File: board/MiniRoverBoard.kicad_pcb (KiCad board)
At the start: 2 copper layers, 103.4 x 63.8 mm, 49 parts, among them J1 DEBUG, Q1 NMOS, Q2 BSS138, U2 OKI, U3 Opamp_Dual, U4 LT1910, U7 ESP32-S2-DEVKITM-1U, U8 Opamp_Dual

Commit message: Corrected 5 volt power grid
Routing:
- net GND: vias 9 -> 17
- added copper zone on F.Cu, net GND
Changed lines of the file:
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@@
+	)
+	(via
+		(at 117.602 70.104)
+		(size 0.6)
+		(drill 0.3)
+		(layers "F.Cu" "B.Cu")
+		(free yes)
+		(net 1)
+	)
+	(via
+		(at 128.27 62.484)
+		(size 0.6)
+		(drill 0.3)
+		(layers "F.Cu" "B.Cu")
+		(free yes)
+		(net 1)
 	)
 	(via
@@
 	)
 	(via
+		(at 122.682 74.422)
+		(size 0.6)
+		(drill 0.3)
+		(layers "F.Cu" "B.Cu")
+		(free yes)
+		(net 1)
+	)
+	(via
+		(at 128.016 55.88)
+		(size 0.6)
+		(drill 0.3)
+		(layers "F.Cu" "B.Cu")
+		(free yes)
+		(net 1)
+	)
+	(via
 		(at 100.838 52.07)
+		(size 0.6)
+		(drill 0.3)
+		(layers "F.Cu" "B.Cu")
+		(free yes)
+		(net 1)
+	)
+	(via
+		(at 146.05 78.74)
 		(size 0.6)
 		(drill 0.3)
@@
 	)
 	(via
+		(at 127 75.184)
+		(size 0.6)
+		(drill 0.3)
+		(layers "F.Cu" "B.Cu")
+		(free yes)
+		(net 1)
+	)
+	(via
 		(at 107.442 52.07)
 		(size 0.6)
@@
 	)
 	(via
+		(at 132.334 66.04)
+		(size 0.6)
+		(drill 0.3)
+		(layers "F.Cu" "B.Cu")
+		(free yes)
+		(net 1)
+	)
+	(via
+		(at 137.16 83.058)
+		(size 0.6)
+		(drill 0.3)
+		(layers "F.Cu" "B.Cu")
+		(free yes)
+		(net 1)
+	)
+	(via
 		(at 58.928 55.626)
 		(size 0.6)
@@
 		(net 3)
 		(net_name "+5V")
+		(layer "F.Cu")
+		(hatch edge 0.5)
+		(priority 3)
+		(connect_pads yes
+			(clearance 0.254)
+		)
+		(min_thickness 0.254)
+		(filled_areas_thickness no)
+		(fill yes
+			(thermal_gap 0.5)
+			(thermal_bridge_width 0.5)
+		)
+		(polygon
+			(pts
+				(xy 117.856 72.136) (xy 117.7055 76.2) (xy 121.158 76.2) (xy 121.666 72.136)
+			)
+		)
+	)
+	(zone
+		(net 1)
+		(net_name "GND")
 		(layer "F.Cu")
 		(hatch edge 0.5)
@@
 		(polygon
 			(pts
-				(xy 117.602 72.282267) (xy 121.412 72.368724) (xy 121.412 76.2) (xy 117.602 76.2)
+				(xy 170.18 72.282267) (xy 173.99 72.368724) (xy 173.99 76.2) (xy 170.18 76.2)
 			)
 		)

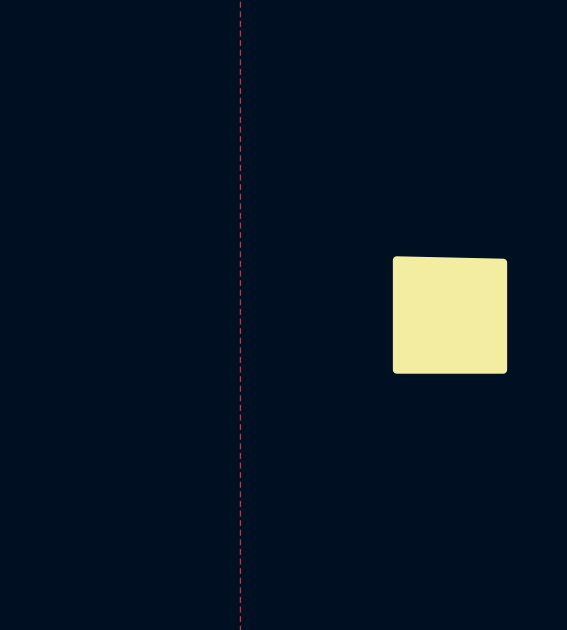
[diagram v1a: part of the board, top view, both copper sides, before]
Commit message: Removed extra 5 volt power grid
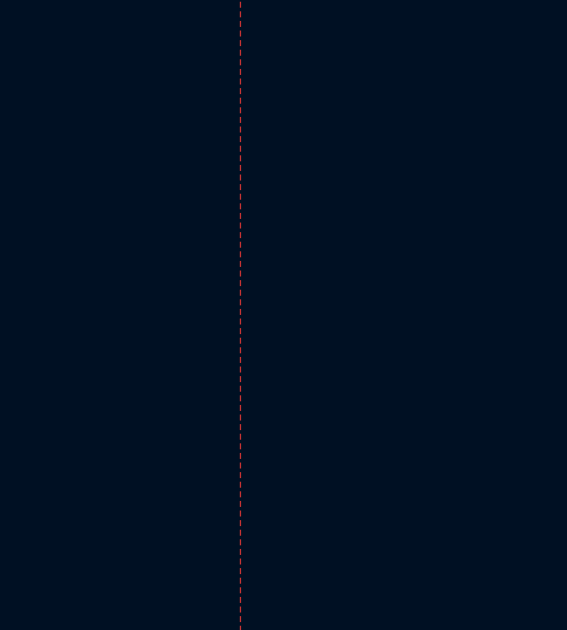
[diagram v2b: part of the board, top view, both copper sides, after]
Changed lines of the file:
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@@
-		)
-	)
-	(zone
-		(net 0)
-		(net_name "")
-		(layer "F.SilkS")
-		(hatch edge 0.5)
-		(connect_pads
-			(clearance 0.254)
-		)
-		(min_thickness 0.25)
-		(filled_areas_thickness no)
-		(fill yes
-			(thermal_gap 0.5)
-			(thermal_bridge_width 0.5)
-		)
-		(polygon
-			(pts
-				(xy 170.18 72.282267) (xy 173.99 72.368724) (xy 173.99 76.2) (xy 170.18 76.2)
-			)
 		)
 	)

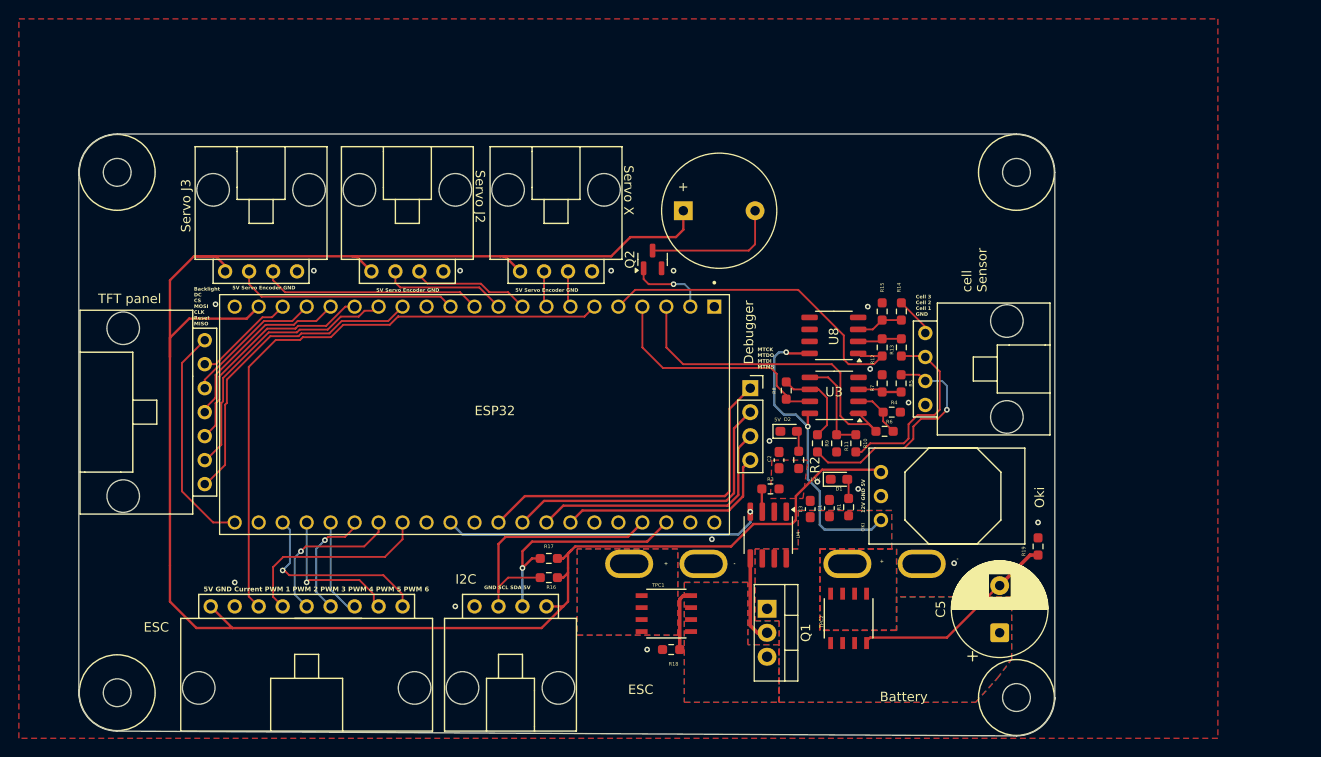
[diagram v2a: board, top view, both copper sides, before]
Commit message: Rotate 2nd MOSFET, ADD Ground Vias, Add Names
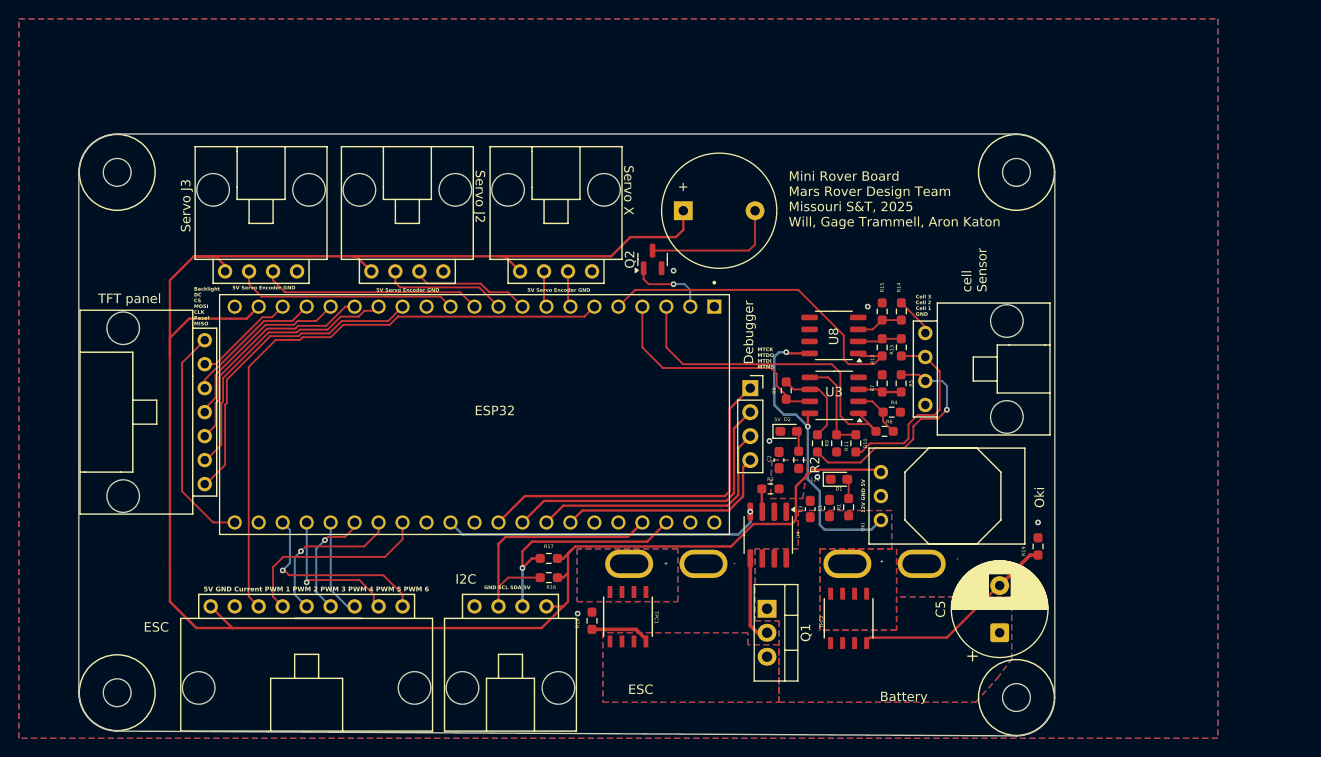
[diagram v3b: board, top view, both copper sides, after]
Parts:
- moved R18 8.92 mm to (98.8, 89.2), turned to -90 degrees
- moved MOSFET1 4.08 mm to (102.6, 88.7), turned to 90 degrees
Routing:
- net +5V: track 211.3 -> 211.9 mm
- net GND: vias 17 -> 6
- added copper zone on B.Cu, net +5V
- added copper zone on B.Cu, net GND
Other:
- outline, holes or cut-outs redrawn
- board text added: "Mini Rover Board Mars Rover Design Team Missouri S&T, 2025 Will, Gage Trammell, Aron Katon"

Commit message: Run DRC
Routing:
- net +12V: track 33.1 -> 24.9 mm
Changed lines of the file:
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@@
 		(tags "resistor handsolder")
 		(property "Reference" "R3"
-			(at 0 1.016 0)
+			(at 0.7385 1.016 0)
 			(layer "F.SilkS")
 			(effects
@@
 		(tags "capacitor handsolder")
 		(property "Reference" "C2"
-			(at 0.146267 -1.016 90)
+			(at 0.635 -1.016 90)
 			(layer "F.SilkS")
 			(effects
@@
 		(tags "resistor handsolder")
 		(property "Reference" "R10"
-			(at 0 1.016 270)
+			(at 0.3556 1.0414 270)
 			(layer "F.SilkS")
 			(effects
@@
 		(tags "resistor handsolder")
 		(property "Reference" "R2"
-			(at -0.53 1.73 90)
+			(at 0.74 0.9934 90)
 			(layer "F.SilkS")
 			(effects
 				(font
-					(size 1 1)
-					(thickness 0.15)
+					(size 0.381 0.381)
+					(thickness 0.09525)
+					(bold yes)
 				)
 			)
@@
 		(tags "resistor handsolder")
 		(property "Reference" "R7"
-			(at -0.508 -1.04 90)
+			(at 0.2286 -1.04 90)
 			(layer "F.SilkS")
 			(effects
@@
 		(tags "resistor handsolder")
 		(property "Reference" "R12"
-			(at 1.27 1.016 90)
+			(at 0.2032 1.016 90)
 			(layer "F.SilkS")
 			(effects
@@
 	)
 	(segment
-		(start 123.444 79.502)
-		(end 128.397 79.502)
-		(width 0.254)
-		(layer "B.Cu")
-		(net 2)
-	)
-	(segment
 		(start 121.666 74.168)
 		(end 122.936 75.438)
@@
 	)
 	(segment
-		(start 122.936 75.438)
-		(end 122.936 78.994)
-		(width 0.254)
-		(layer "B.Cu")
-		(net 2)
-	)
-	(segment
-		(start 122.936 78.994)
-		(end 123.444 79.502)
-		(width 0.254)
-		(layer "B.Cu")
-		(net 2)
-	)
-	(segment
 		(start 118.618 60.706)
 		(end 118.11 61.214)
@@
 	)
 	(segment
-		(start 121.666 68.58)
-		(end 121.666 74.168)
+		(start 122.936 75.438)
+		(end 122.936 77.9018)
 		(width 0.254)
 		(layer "B.Cu")
@@
 	)
 	(segment
-		(start 128.397 79.502)
-		(end 129.413 78.486)
+		(start 121.666 68.58)
+		(end 121.666 74.168)
 		(width 0.254)
 		(layer "B.Cu")

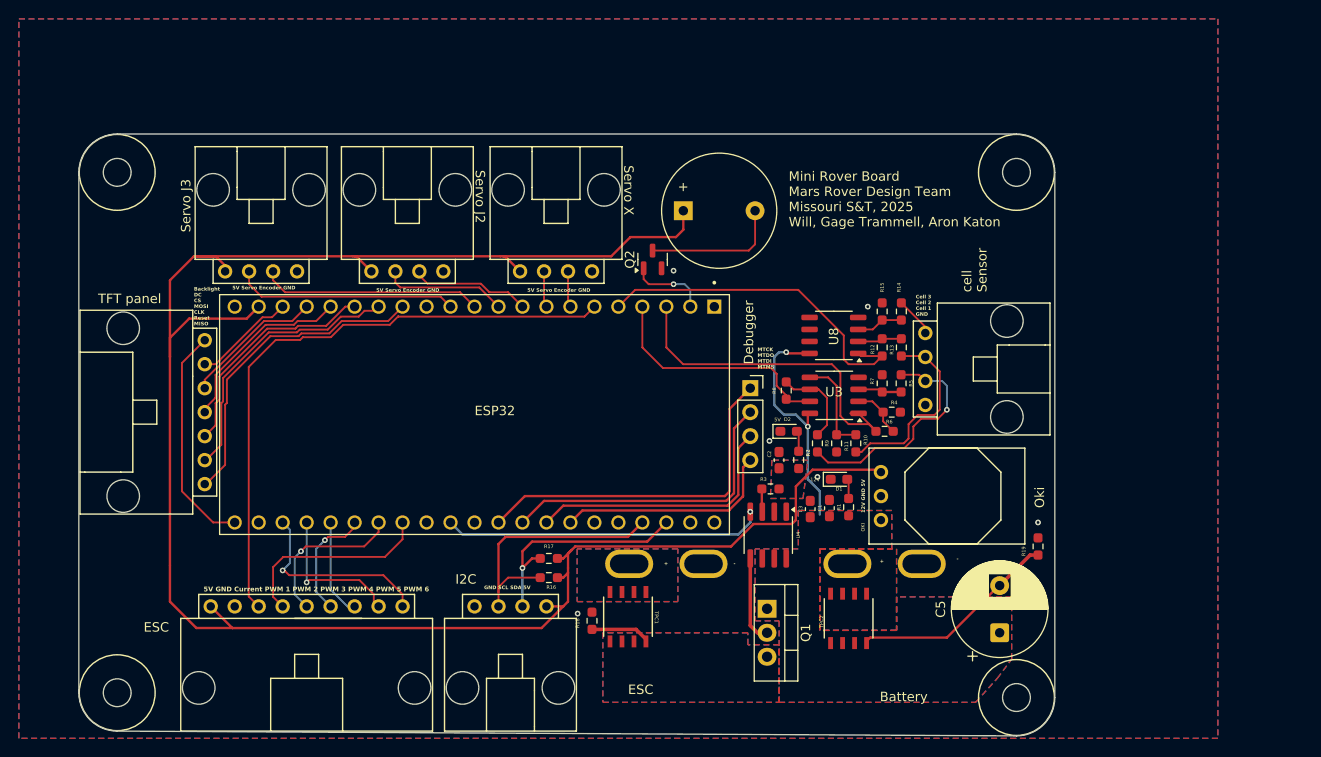
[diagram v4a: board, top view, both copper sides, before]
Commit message: Add net for andersons
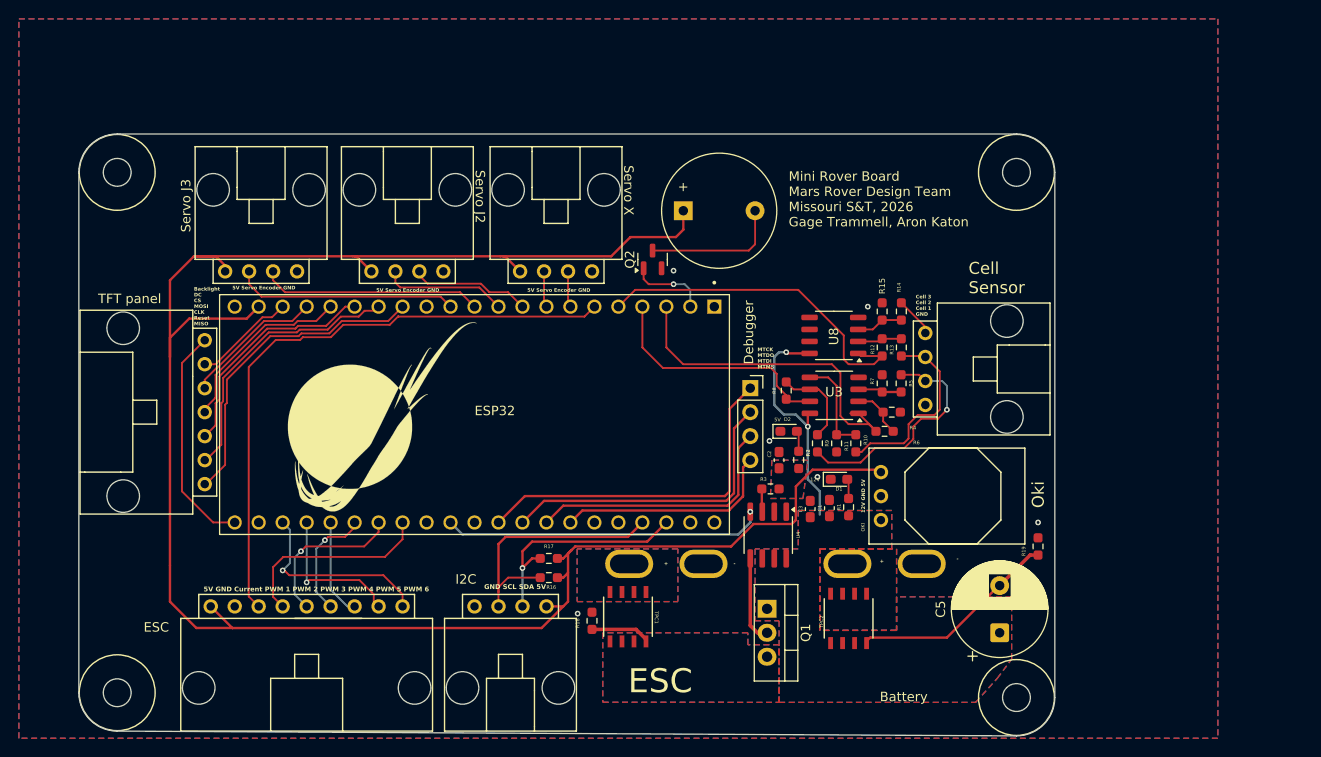
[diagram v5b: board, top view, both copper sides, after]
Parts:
- added G***: LOGO, MRDT_Silkscreens:0_MRDT_Logo_20mm, F.Cu at (76.6, 67.6)
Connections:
- Conn2 pad 4: (no net) -> Net-(Conn2B-V+Log)
- Conn3 pad 4: (no net) -> Net-(Conn3B-V+Log)
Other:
- board text added: "Cell Sensor"
- board text added: "Mini Rover Board Mars Rover Design Team Missouri S&T, 2026 Gage Trammell, Aron Katon"
- board text removed: "Mini Rover Board Mars Rover Design Team Missouri S&T, 2025 Will, Gage Trammell, Aron Katon"
- board text removed: "cell Sensor"

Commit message: fixed font size
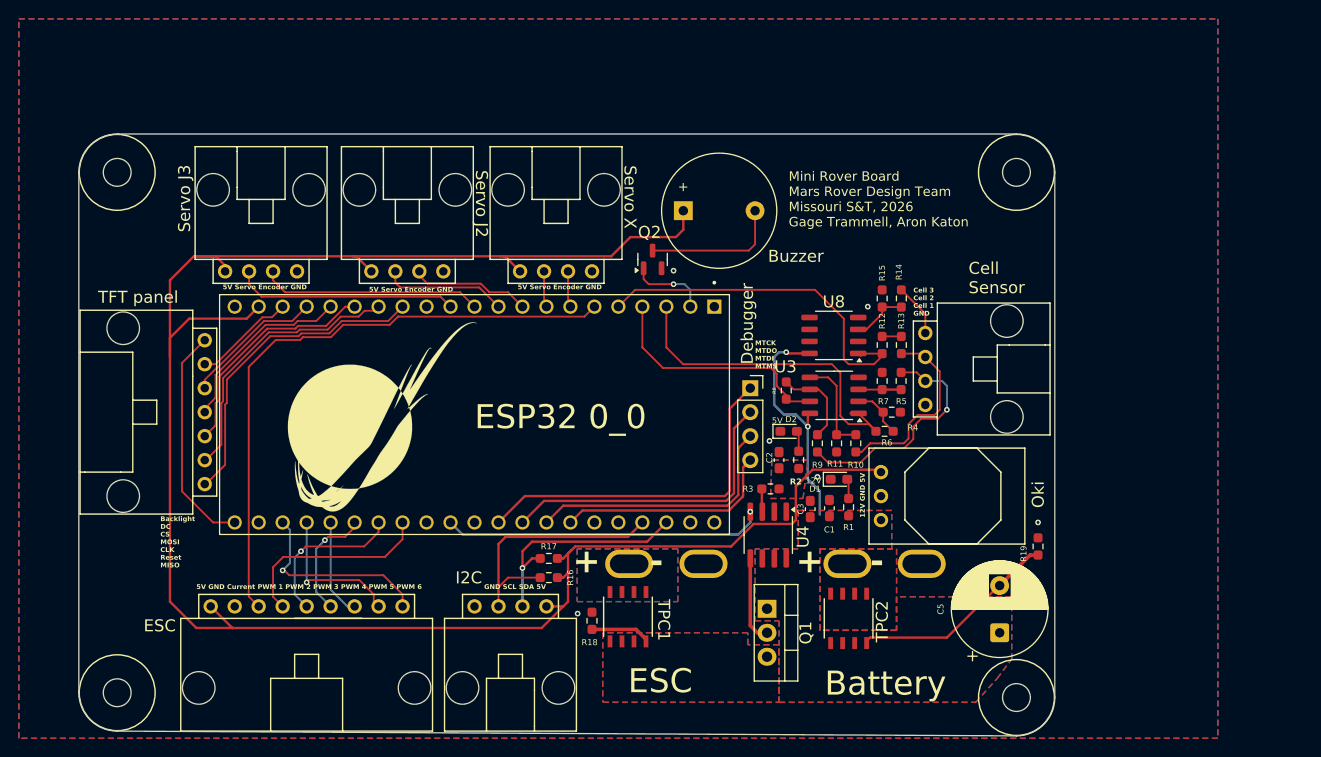
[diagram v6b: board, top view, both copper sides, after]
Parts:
- moved R14 1.37 mm to (131.6, 55.0)
- moved R15 1.37 mm to (129.5, 55.0)
- moved R12 0.25 mm to (129.5, 59.9)
- moved R13 0.25 mm to (131.6, 59.9)
- moved R5 0.25 mm to (131.5, 63.8)
- moved R7 0.25 mm to (129.5, 63.8)
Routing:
- net Net-(U8A--): track 4.69 -> 2.42 mm
- net CELL_SENSE_3: track 36.7 -> 38.3 mm
- net CELL3: track 4.25 -> 5.62 mm
- net Net-(U8A-+): track 4.98 -> 5.96 mm
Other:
- board text added: "ESP32 0_0"
- board text removed: "ESP32"

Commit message: Seperate labels
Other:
- board text added: "1"
- board text added: "2"
- board text added: "3"
- board text added: "4"
- board text added: "5"
- board text added: "6"
- board text added: "C"
- board text added: "GND"
- board text removed: "5V GND Current PWM 1 PWM 2 PWM 3 PWM 4 PWM 5 PWM 6"
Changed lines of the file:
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@@
 				(font
 					(size 0.635 0.635)
-					(thickness 0.09525)
+					(thickness 0.079375)
 				)
 			)
@@
 				(font
 					(size 0.635 0.635)
-					(thickness 0.09525)
+					(thickness 0.079375)
 				)
 			)
@@
 				(font
 					(size 0.635 0.635)
-					(thickness 0.09525)
+					(thickness 0.079375)
 				)
 			)
@@
 		(layer "Edge.Cuts")
 	)
+	(gr_text "5"
+		(at 75.692 86.106 0)
+		(layer "F.SilkS")
+		(effects
+			(font
+				(size 0.508 0.508)
+				(thickness 0.1016)
+				(bold yes)
+			)
+			(justify left bottom)
+		)
+	)
 	(gr_text "Servo J2\n"
 		(at 86.36 41.402 270)
@@
 			(font
 				(size 2.54 2.54)
-				(thickness 0.1)
+				(thickness 0.3175)
 			)
 			(justify left bottom)
@@
 		)
 	)
+	(gr_text "1"
+		(at 65.532 86.106 0)
+		(layer "F.SilkS")
+		(effects
+			(font
+				(size 0.508 0.508)
+				(thickness 0.1016)
+				(bold yes)
+			)
+			(justify left bottom)
+		)
+	)
+	(gr_text "6"
+		(at 78.74 86.106 0)
+		(layer "F.SilkS")
+		(effects
+			(font
+				(size 0.508 0.508)
+				(thickness 0.1016)
+				(bold yes)
+			)
+			(justify left bottom)
+		)
+	)
 	(gr_text "+"
 		(at 120.396 84.328 0)
@@
 		)
 	)
+	(gr_text "C"
+		(at 62.738 85.852 0)
+		(layer "F.SilkS")
+		(effects
+			(font
+				(size 0.508 0.508)
+				(thickness 0.1016)
+				(bold yes)
+			)
+			(justify left bottom)
+		)
+	)
 	(gr_text "5V\n"
 		(at 117.856 68.326 0)
@@
 		)
 	)
+	(gr_text "GND"
+		(at 60.198 85.852 0)
+		(layer "F.SilkS")
+		(effects
+			(font
+				(size 0.508 0.508)
+				(thickness 0.1016)
+				(bold yes)
+			)
+			(justify left bottom)
+		)
+	)
 	(gr_text "R11\n"
 		(at 123.698 72.898 0)
@@
 		)
 	)
-	(gr_text "5V GND Current PWM 1 PWM 2 PWM 3 PWM 4 PWM 5 PWM 6"
-		(at 56.896 85.852 0)
+	(gr_text "5V"
+		(at 57.912 85.852 0)
 		(layer "F.SilkS")
 		(effects
@@
 		)
 	)
+	(gr_text "3"
+		(at 70.358 86.106 0)
+		(layer "F.SilkS")
+		(effects
+			(font
+				(size 0.508 0.508)
+				(thickness 0.1016)
+				(bold yes)
+			)
+			(justify left bottom)
+		)
+	)
 	(gr_text "-\n"
 		(at 128.27 84.328 0)
@@
 			(font
 				(size 2.54 2.54)
-				(thickness 0.1)
+				(thickness 0.3175)
+			)
+			(justify left bottom)
+		)
+	)
+	(gr_text "2"
+		(at 68.072 86.106 0)
+		(layer "F.SilkS")
+		(effects
+			(font
+				(size 0.508 0.508)
+				(thickness 0.1016)
+				(bold yes)
 			)
 			(justify left bottom)
@@
 			(font
 				(size 1.27 1.27)
-				(thickness 0.1)
+				(thickness 0.15875)
+			)
+			(justify left bottom)
+		)
+	)
+	(gr_text "4"
+		(at 73.152 86.106 0)
+		(layer "F.SilkS")
+		(effects
+			(font
+				(size 0.508 0.508)
+				(thickness 0.1016)
+				(bold yes)
 			)
 			(justify left bottom)
